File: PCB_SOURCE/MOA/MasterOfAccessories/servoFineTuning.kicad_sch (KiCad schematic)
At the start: 4 parts, among them J801 Conn_01x04_Socket

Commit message: added some files, but mainly this is to update hex file of OSSD
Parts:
- renumbered C802 to C701, C803 to C702, J801 to J701, R801 to R701
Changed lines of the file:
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@@
 		(on_board yes)
 		(dnp no)
-		(property "Reference" "R801"
+		(property "Reference" "R701"
 			(at 102.87 114.3 0)
 			(effects
@@
 			(project "MasterOfAccessories"
 				(path "/d28c018f-83ab-41ca-9c80-395a46ff97ad/3cd81a08-dbfb-46cf-8c7b-9fac5c669f8b"
-					(reference "R801")
+					(reference "R701")
 					(unit 1)
 				)
@@
 		(dnp no)
 		(fields_autoplaced yes)
-		(property "Reference" "#PWR0806"
+		(property "Reference" "#PWR0705"
 			(at 115.57 134.62 0)
 			(effects
@@
 			(project "MasterOfAccessories"
 				(path "/d28c018f-83ab-41ca-9c80-395a46ff97ad/3cd81a08-dbfb-46cf-8c7b-9fac5c669f8b"
-					(reference "#PWR0806")
+					(reference "#PWR0705")
 					(unit 1)
 				)
@@
 		(dnp no)
 		(fields_autoplaced yes)
-		(property "Reference" "#PWR0805"
+		(property "Reference" "#PWR0701"
 			(at 88.9 114.3 0)
 			(effects
@@
 			(project "MasterOfAccessories"
 				(path "/d28c018f-83ab-41ca-9c80-395a46ff97ad/3cd81a08-dbfb-46cf-8c7b-9fac5c669f8b"
-					(reference "#PWR0805")
+					(reference "#PWR0701")
 					(unit 1)
 				)
@@
 		(dnp no)
 		(fields_autoplaced yes)
-		(property "Reference" "#PWR0804"
+		(property "Reference" "#PWR0703"
 			(at 109.22 114.3 0)
 			(effects
@@
 			(project "MasterOfAccessories"
 				(path "/d28c018f-83ab-41ca-9c80-395a46ff97ad/3cd81a08-dbfb-46cf-8c7b-9fac5c669f8b"
-					(reference "#PWR0804")
+					(reference "#PWR0703")
 					(unit 1)
 				)
@@
 		(on_board yes)
 		(dnp no)
-		(property "Reference" "C803"
+		(property "Reference" "C702"
 			(at 91.44 114.3 0)
 			(effects
@@
 			(project "MasterOfAccessories"
 				(path "/d28c018f-83ab-41ca-9c80-395a46ff97ad/3cd81a08-dbfb-46cf-8c7b-9fac5c669f8b"
-					(reference "C803")
+					(reference "C702")
 					(unit 1)
 				)
@@
 		(on_board yes)
 		(dnp no)
-		(property "Reference" "J801"
+		(property "Reference" "J701"
 			(at 123.19 124.4601 0)
 			(effects
@@
 			(project "MasterOfAccessories"
 				(path "/d28c018f-83ab-41ca-9c80-395a46ff97ad/3cd81a08-dbfb-46cf-8c7b-9fac5c669f8b"
-					(reference "J801")
+					(reference "J701")
 					(unit 1)
 				)
@@
 		(dnp no)
 		(fields_autoplaced yes)
-		(property "Reference" "#PWR0807"
+		(property "Reference" "#PWR0702"
 			(at 99.06 114.3 0)
 			(effects
@@
 			(project "MasterOfAccessories"
 				(path "/d28c018f-83ab-41ca-9c80-395a46ff97ad/3cd81a08-dbfb-46cf-8c7b-9fac5c669f8b"
-					(reference "#PWR0807")
+					(reference "#PWR0702")
 					(unit 1)
 				)
@@
 		(on_board yes)
 		(dnp no)
-		(property "Reference" "C802"
+		(property "Reference" "C701"
 			(at 80.01 114.3 0)
 			(effects
@@
 			(project "MasterOfAccessories"
 				(path "/d28c018f-83ab-41ca-9c80-395a46ff97ad/3cd81a08-dbfb-46cf-8c7b-9fac5c669f8b"
-					(reference "C802")
+					(reference "C701")
 					(unit 1)
 				)
@@
 		(dnp no)
 		(fields_autoplaced yes)
-		(property "Reference" "#PWR0803"
+		(property "Reference" "#PWR0704"
 			(at 115.57 114.3 0)
 			(effects
@@
 			(project "MasterOfAccessories"
 				(path "/d28c018f-83ab-41ca-9c80-395a46ff97ad/3cd81a08-dbfb-46cf-8c7b-9fac5c669f8b"
-					(reference "#PWR0803")
-					(unit 1)
-				)
+					(reference "#PWR0704")
+					(unit 1)
+				)

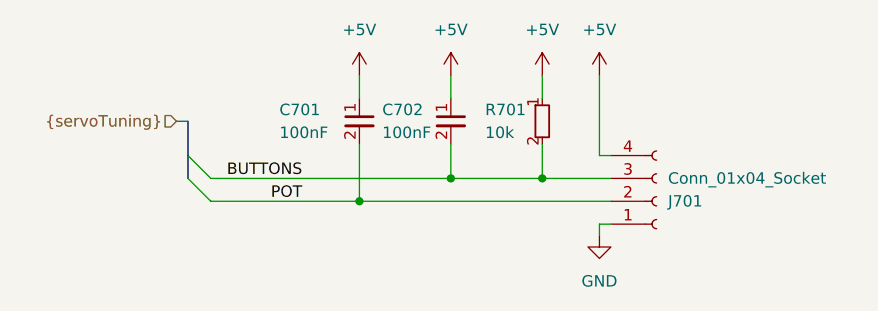
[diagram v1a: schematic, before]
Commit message: fixed bug in ahob program among others
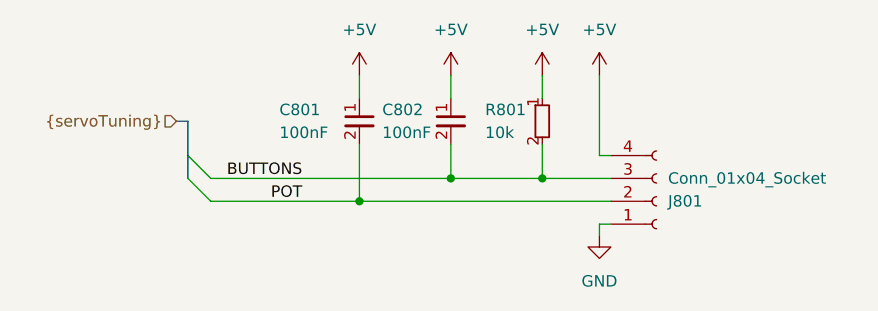
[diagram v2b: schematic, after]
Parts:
- renumbered C701 to C801, C702 to C802, J701 to J801, R701 to R801
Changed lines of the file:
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@@
 	(label "BUTTONS"
 		(at 82.55 121.92 180)
-		(fields_autoplaced yes)
 		(effects
 			(font
@@
 	(label "POT"
 		(at 82.55 124.46 180)
-		(fields_autoplaced yes)
 		(effects
 			(font
@@
 		(shape input)
 		(at 68.58 115.57 180)
-		(fields_autoplaced yes)
 		(effects
 			(font
@@
 		(on_board yes)
 		(dnp no)
-		(property "Reference" "R701"
+		(property "Reference" "R801"
 			(at 102.87 114.3 0)
 			(effects
@@
 			(project "MasterOfAccessories"
 				(path "/d28c018f-83ab-41ca-9c80-395a46ff97ad/3cd81a08-dbfb-46cf-8c7b-9fac5c669f8b"
-					(reference "R701")
+					(reference "R801")
 					(unit 1)
 				)
@@
 		(dnp no)
 		(fields_autoplaced yes)
-		(property "Reference" "#PWR0705"
+		(property "Reference" "#PWR0805"
 			(at 115.57 134.62 0)
 			(effects
@@
 			(project "MasterOfAccessories"
 				(path "/d28c018f-83ab-41ca-9c80-395a46ff97ad/3cd81a08-dbfb-46cf-8c7b-9fac5c669f8b"
-					(reference "#PWR0705")
+					(reference "#PWR0805")
 					(unit 1)
 				)
@@
 		(dnp no)
 		(fields_autoplaced yes)
-		(property "Reference" "#PWR0701"
+		(property "Reference" "#PWR0801"
 			(at 88.9 114.3 0)
 			(effects
@@
 			(project "MasterOfAccessories"
 				(path "/d28c018f-83ab-41ca-9c80-395a46ff97ad/3cd81a08-dbfb-46cf-8c7b-9fac5c669f8b"
-					(reference "#PWR0701")
+					(reference "#PWR0801")
 					(unit 1)
 				)
@@
 		(dnp no)
 		(fields_autoplaced yes)
-		(property "Reference" "#PWR0703"
+		(property "Reference" "#PWR0803"
 			(at 109.22 114.3 0)
 			(effects
@@
 			(project "MasterOfAccessories"
 				(path "/d28c018f-83ab-41ca-9c80-395a46ff97ad/3cd81a08-dbfb-46cf-8c7b-9fac5c669f8b"
-					(reference "#PWR0703")
+					(reference "#PWR0803")
 					(unit 1)
 				)
@@
 		(on_board yes)
 		(dnp no)
-		(property "Reference" "C702"
+		(property "Reference" "C802"
 			(at 91.44 114.3 0)
 			(effects
@@
 			(project "MasterOfAccessories"
 				(path "/d28c018f-83ab-41ca-9c80-395a46ff97ad/3cd81a08-dbfb-46cf-8c7b-9fac5c669f8b"
-					(reference "C702")
+					(reference "C802")
 					(unit 1)
 				)
@@
 		(on_board yes)
 		(dnp no)
-		(property "Reference" "J701"
+		(property "Reference" "J801"
 			(at 123.19 124.4601 0)
 			(effects
@@
 			(project "MasterOfAccessories"
 				(path "/d28c018f-83ab-41ca-9c80-395a46ff97ad/3cd81a08-dbfb-46cf-8c7b-9fac5c669f8b"
-					(reference "J701")
+					(reference "J801")
 					(unit 1)
 				)
@@
 		(dnp no)
 		(fields_autoplaced yes)
-		(property "Reference" "#PWR0702"
+		(property "Reference" "#PWR0802"
 			(at 99.06 114.3 0)
 			(effects
@@
 			(project "MasterOfAccessories"
 				(path "/d28c018f-83ab-41ca-9c80-395a46ff97ad/3cd81a08-dbfb-46cf-8c7b-9fac5c669f8b"
-					(reference "#PWR0702")
+					(reference "#PWR0802")
 					(unit 1)
 				)
@@
 		(on_board yes)
 		(dnp no)
-		(property "Reference" "C701"
+		(property "Reference" "C801"
 			(at 80.01 114.3 0)
 			(effects
@@
 			(project "MasterOfAccessories"
 				(path "/d28c018f-83ab-41ca-9c80-395a46ff97ad/3cd81a08-dbfb-46cf-8c7b-9fac5c669f8b"
-					(reference "C701")
+					(reference "C801")
 					(unit 1)
 				)
@@
 		(dnp no)
 		(fields_autoplaced yes)
-		(property "Reference" "#PWR0704"
+		(property "Reference" "#PWR0804"
 			(at 115.57 114.3 0)
 			(effects
@@
 			(project "MasterOfAccessories"
 				(path "/d28c018f-83ab-41ca-9c80-395a46ff97ad/3cd81a08-dbfb-46cf-8c7b-9fac5c669f8b"
-					(reference "#PWR0704")
-					(unit 1)
-				)
+					(reference "#PWR0804")
+					(unit 1)
+				)
